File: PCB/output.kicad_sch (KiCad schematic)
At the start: 0 parts

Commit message: Cleaned up the schematic and got started on assigning all the footprints to the symbols
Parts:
- added C16, C17: 0.01 µF, Capacitor_THT:C_Radial_D5.0mm_H5.0mm_P2.00mm, symbol Device:C
- added C18, C19: 0.1 µF, Capacitor_THT:C_Radial_D5.0mm_H5.0mm_P2.00mm, symbol Device:C
- added R37: 1k, Resistor_THT:R_Axial_DIN0207_L6.3mm_D2.5mm_P7.62mm_Horizontal, symbol Device:R
- added R38: 100k, Resistor_THT:R_Axial_DIN0207_L6.3mm_D2.5mm_P7.62mm_Horizontal, symbol Device:R
- added R39: 10k, Resistor_THT:R_Axial_DIN0207_L6.3mm_D2.5mm_P7.62mm_Horizontal, symbol Device:R
- added SW7: SW_SPDT, Button_Switch_SMD:SW_SPDT_CK_JS102011SAQN, symbol Switch:SW_SPDT
- added U31: LM555xM, Package_SO:SOIC-8_3.9x4.9mm_P1.27mm, symbol Timer:LM555xM
- added U32: 74LS76, symbol 74xx:74LS76
- added U33: 74LS139, Package_DIP:DIP-16_W7.62mm, symbol 74xx:74LS139
- added U34, U35, U36, U37: D148K, Display_7Segment:D1X8K, symbol Display_Character:D148K
- added U38: 74LS273, symbol 74xx:74LS273
- added U39: 74LS08, symbol 74xx:74LS08
- added U40: AT28C64B-15PU, AT28C64B_15PU:DIP1555W45P254L3733H482Q28, symbol AT28C64B-15PU:AT28C64B-15PU
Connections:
- new net: C16.1, R38.1, U31.2 (TR), U31.6 (THR)
- new net: C17.1, U31.5 (CV)
- new net: U32.14 (~{Q}), U32.6 (C), U33.2 (A0), U40.25 (A8)
- new net: U32.10 (~{Q}), U33.3 (A1), U40.24 (A9)
- new net: U33.4 (O0), U35.3 (CC), U35.8 (CC)
- new net: U33.5 (O1), U37.3 (CC), U37.8 (CC)
- new net: U33.6 (O2), U36.3 (CC), U36.8 (CC)
- new net: U33.7 (O3), U34.3 (CC), U34.8 (CC)
- new net: U34.1 (E), U35.1 (E), U36.1 (E), U37.1 (E), U40.13 (I/O2)
- new net: U34.10 (G), U35.10 (G), U36.10 (G), U37.10 (G), U40.11 (I/O0)
- new net: U34.2 (D), U35.2 (D), U36.2 (D), U37.2 (D), U40.15 (I/O3)
- new net: U34.4 (C), U35.4 (C), U36.4 (C), U37.4 (C), U40.16 (I/O4)
- new net: U34.5 (DP), U35.5 (DP), U36.5 (DP), U37.5 (DP), U40.19 (I/O7)
- new net: U34.6 (B), U35.6 (B), U36.6 (B), U37.6 (B), U40.17 (I/O5)
- new net: U34.7 (A), U35.7 (A), U36.7 (A), U37.7 (A), U40.18 (I/O6)
- new net: U34.9 (F), U35.9 (F), U36.9 (F), U37.9 (F), U40.12 (I/O1)
- new net: U31.3 (Q), U32.1 (C)
- new net: R37.2, R38.2, U31.7 (DIS)
- new net: R39.1, SW7.1 (A)
- new net: U38.11 (Cp), U39.3
- new net: U38.2 (Q0), U40.10 (A0)
- new net: SW7.2 (B), U40.21 (A10)
- new net: U38.19 (Q7), U40.3 (A7)
- new net: U38.16 (Q6), U40.4 (A6)
- new net: U38.15 (Q5), U40.5 (A5)
- new net: U38.12 (Q4), U40.6 (A4)
- new net: U38.9 (Q3), U40.7 (A3)
- new net: U38.6 (Q2), U40.8 (A2)
- new net: U38.5 (Q1), U40.9 (A1)
- new net 0I: U39.1
- new net BUS_0: U38.3 (D0)
- new net BUS_1: U38.4 (D1)
- new net BUS_2: U38.7 (D2)
- new net BUS_3: U38.8 (D3)
- new net BUS_4: U38.13 (D4)
- new net BUS_5: U38.14 (D5)
- new net BUS_6: U38.17 (D6)
- new net BUS_7: U38.18 (D7)
- new net CLK: U39.2
- new net GND: C16.2, C17.2, C18.2, C19.2, R39.2, U31.1 (GND), U32.13 (GND), U33.8 (GND), U38.10 (GND), U39.7 (GND), U40.14 (GND), U40.2 (A12), U40.20 (~{CE}), U40.22 (~{OE}), U40.23 (A11)
- new net VCC: C18.1, C19.1, R37.1, SW7.3 (C), U31.8 (VCC), U32.12 (K), U32.16 (K), U32.2 (~{S}), U32.3 (~{R}), U32.4 (J), U32.5 (VCC), U32.7 (~{S}), U32.8 (~{R}), U32.9 (J), U33.16 (VCC), U38.20 (VCC), U39.14 (VCC), U40.27 (~{WE}), U40.28 (VCC)
- new net ~{CLR}: U38.1 (~{Mr})
- no-connect marks 0 -> 2

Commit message: added more models to work with on my pcb
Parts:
- U32: footprint (none) -> Package_DIP:DIP-16_W7.62mm
- U38: footprint (none) -> Custom:DIP254P762X508-20
- U39: footprint (none) -> Custom:N14
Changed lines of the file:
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@@
 			)
 		)
-		(property "Footprint" ""
+		(property "Footprint" "Package_DIP:DIP-16_W7.62mm"
 			(at 121.92 41.91 0)
 			(effects
@@
 			)
 		)
-		(property "Footprint" ""
+		(property "Footprint" "Custom:N14"
 			(at 36.83 125.73 0)
 			(effects
@@
 			)
 		)
-		(property "Footprint" ""
+		(property "Footprint" "Package_DIP:DIP-16_W7.62mm"
 			(at 91.44 39.37 0)
 			(effects
@@
 			)
 		)
-		(property "Footprint" ""
+		(property "Footprint" "Package_DIP:DIP-16_W7.62mm"
 			(at 63.5 191.77 0)
 			(effects
@@
 			)
 		)
-		(property "Footprint" ""
+		(property "Footprint" "Custom:DIP254P762X508-20"
 			(at 67.31 105.41 0)
 			(effects
@@
 			)
 		)
-		(property "Footprint" ""
+		(property "Footprint" "Custom:N14"
 			(at 163.83 177.8 0)
 			(effects

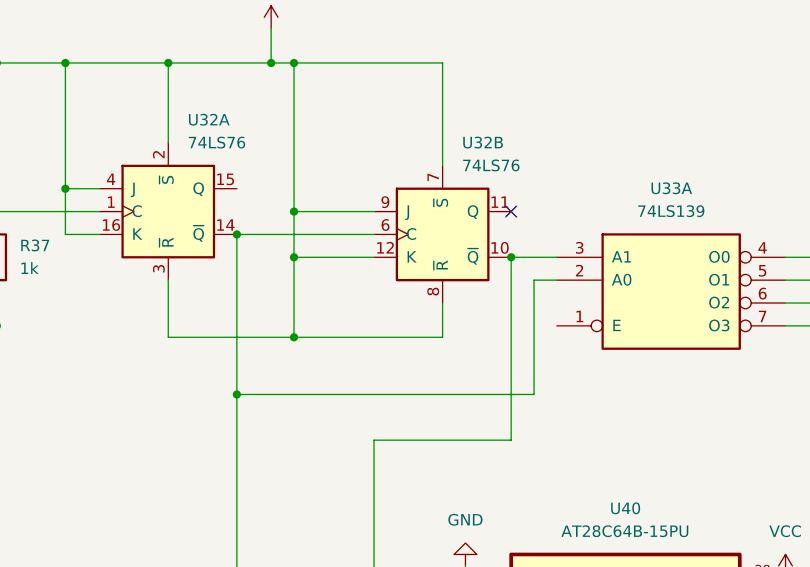
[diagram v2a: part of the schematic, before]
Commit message: Fixed a bunch of ERC errors so know there is only one remaining.
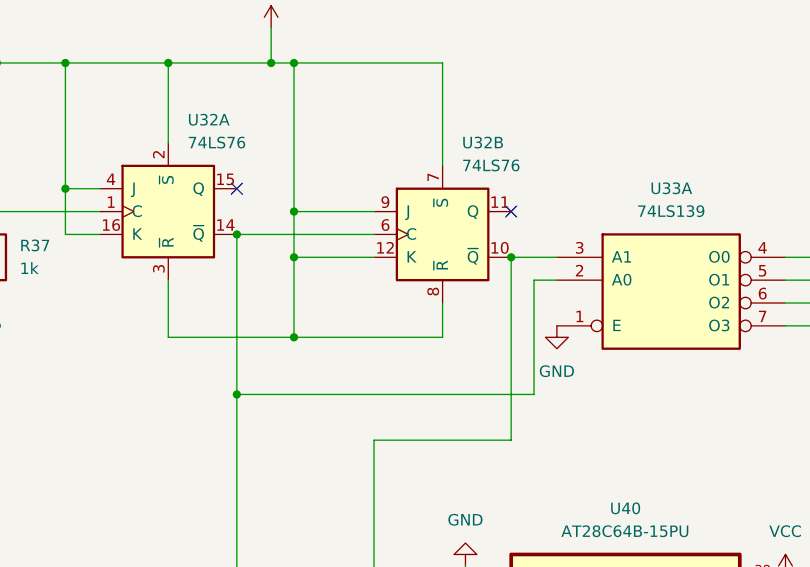
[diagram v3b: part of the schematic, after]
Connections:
- net GND: now also U33.1 (E)
- no-connect marks 2 -> 3
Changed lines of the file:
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@@
+	)
+	(no_connect
+		(at 99.06 36.83)
 	)
 	(no_connect
@@
 					(unit 1)
 				)
+			)
+		)
+	)
+	(symbol
+		(lib_id "power:GND")
+		(at 134.62 52.07 0)
+		(unit 1)
+		(exclude_from_sim no)
+		(in_bom yes)
+		(on_board yes)
+		(dnp no)
+		(fields_autoplaced yes)
+		(property "Reference" "#PWR0157"
+			(at 134.62 58.42 0)
+			(effects
+				(font
+					(size 1.27 1.27)
+				)
+				(hide yes)
+			)
+		)
+		(property "Value" "GND"
+			(at 134.62 57.15 0)
+			(effects
+				(font
+					(size 1.27 1.27)
+				)
+			)
+		)
+		(property "Footprint" ""
+			(at 134.62 52.07 0)
+			(effects
+				(font
+					(size 1.27 1.27)
+				)
+				(hide yes)
+			)
+		)
+		(property "Datasheet" ""
+			(at 134.62 52.07 0)
+			(effects
+				(font
+					(size 1.27 1.27)
+				)
+				(hide yes)
+			)
+		)
+		(property "Description" "Power symbol creates a global label with name \"GND\" , ground"
+			(at 134.62 52.07 0)
+			(effects
+				(font
+					(size 1.27 1.27)
+				)
+				(hide yes)
+			)
+		)
+		(pin "1"
+		)
+		(instances
+			(project ""
+				(path "/48633dea-2de9-4b6f-aeff-2ee54233f918/ce70f6b7-a244-4015-92a7-c586e7888688"
+					(reference "#PWR0157")
+					(unit 1)
+				)

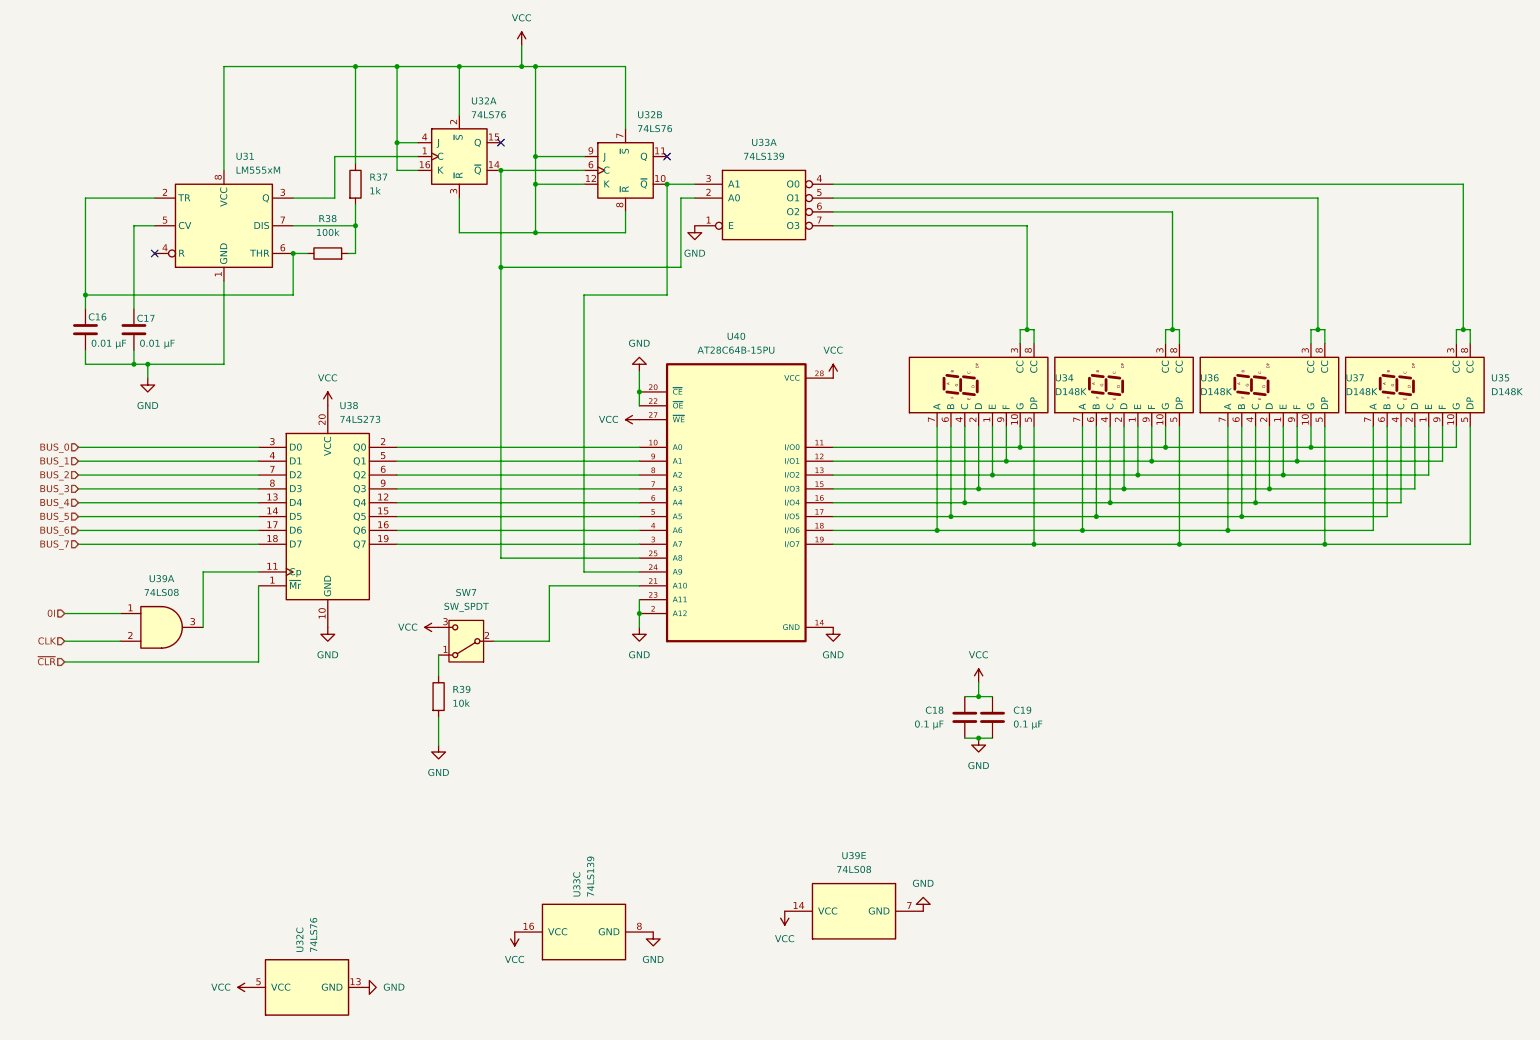
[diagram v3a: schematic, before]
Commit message: Add decupling caps and reroute pcb. Updated BOM to match new number of caps
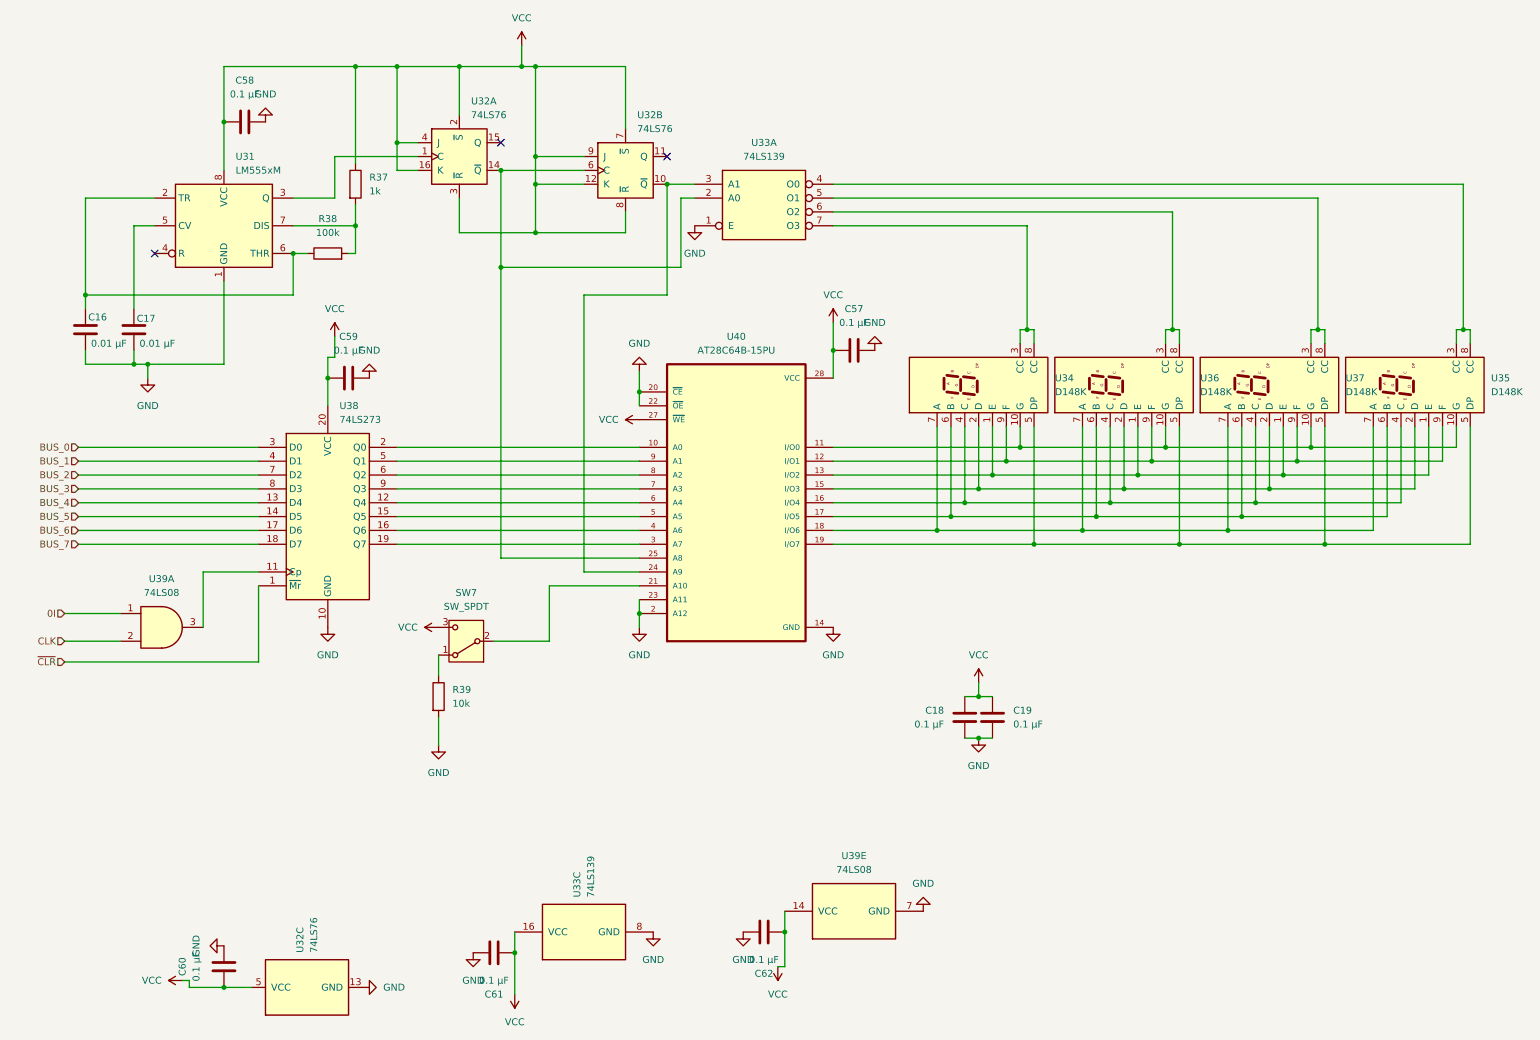
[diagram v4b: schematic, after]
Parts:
- added C57, C58, C59, C60, C61, C62: 0.1 µF, Capacitor_THT:C_Radial_D5.0mm_H5.0mm_P2.00mm, symbol Device:C
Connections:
- net GND: now also C57.2, C58.2, C59.2, C60.2, C61.2, C62.2
- net VCC: now also C57.1, C58.1, C59.1, C60.1, C61.1, C62.1

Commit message: Redoing PCB layout and fixed some signal flow convention errors
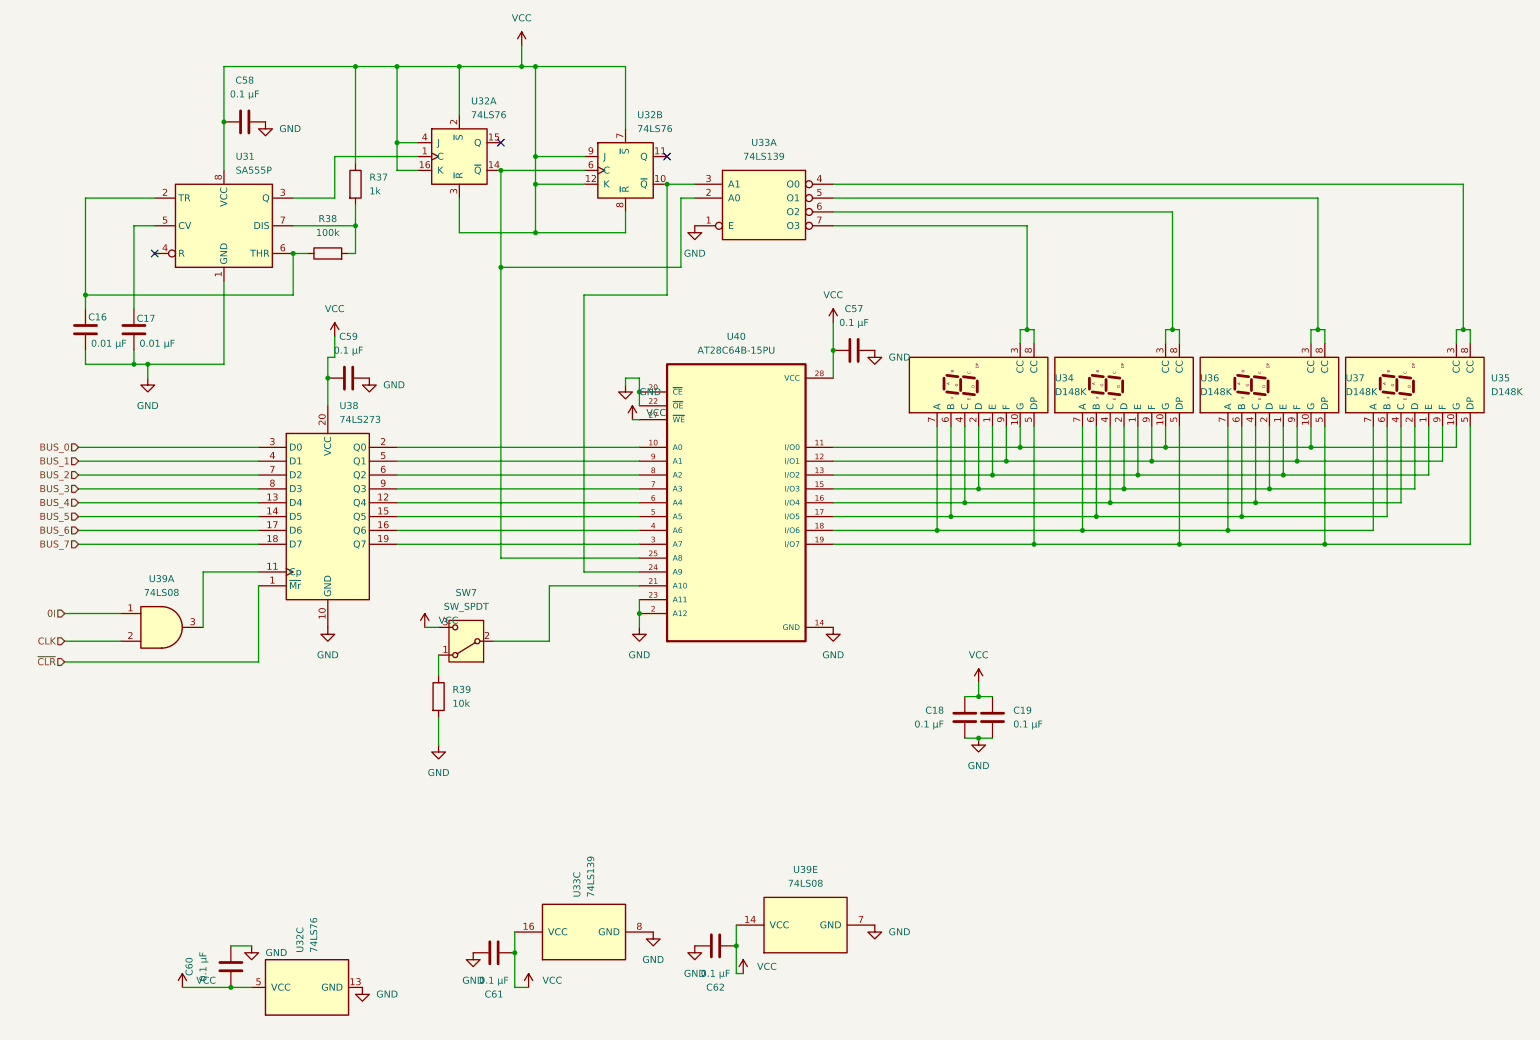
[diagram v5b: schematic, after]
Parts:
- removed U31: LM555xM, Package_SO:SOIC-8_3.9x4.9mm_P1.27mm, symbol Timer:LM555xM
- added U31: SA555P, Package_DIP:DIP-8_W7.62mm, symbol Timer:SA555P
- U40: footprint AT28C64B_15PU:DIP1555W45P254L3733H482Q28 -> Package_DIP:DIP-28_W15.24mm
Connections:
- net GND: now also U31.1 (GND)
- net VCC: now also U31.8 (VCC)
- net at C16.1, R38.1: now also U31.2 (TR), U31.6 (THR)
- net at C17.1: now also U31.5 (CV)
- net at U32.1 (C): now also U31.3 (Q)
- net at R37.2, R38.2: now also U31.7 (DIS)
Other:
- moved on the sheet: C60, C62, U39E

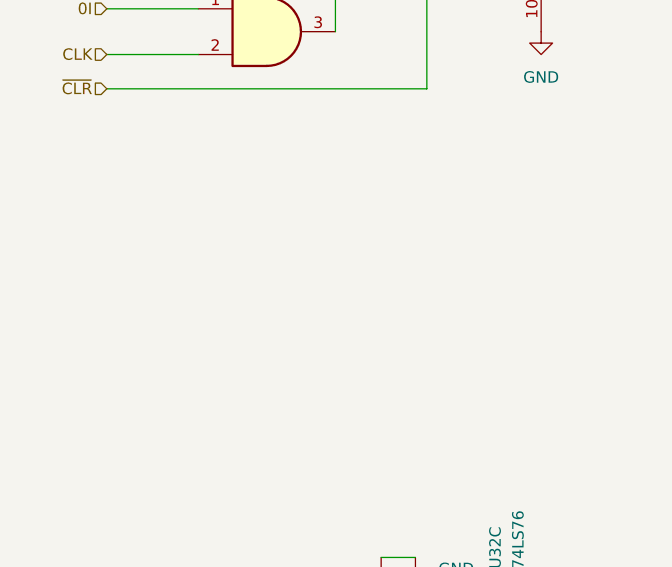
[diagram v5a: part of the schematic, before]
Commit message: update BOM to reflect cheaper prices and more acurate item ammounts, also worked on laying out the PCB.
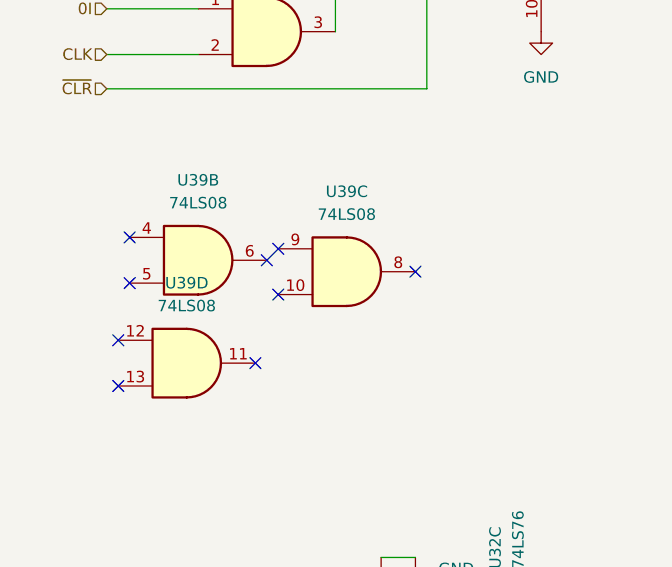
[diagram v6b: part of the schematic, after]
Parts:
- SW7: footprint Button_Switch_SMD:SW_SPDT_CK_JS102011SAQN -> Button_Switch_THT:SW_Slide-03_Wuerth-WS-SLTV_10x2.5x6.4_P2.54mm
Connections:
- no-connect marks 3 -> 12

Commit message: backing up before routing for easily going back if i mess up
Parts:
- added unit 3 of U39
- added unit 4 of U39
- added unit 2 of U39
